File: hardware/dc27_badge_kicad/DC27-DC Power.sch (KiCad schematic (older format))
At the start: 21 parts, among them SW401 POWER ON, U401 MCP73831-2-OT, U402 LM1117-3.3, U403 MAX17043

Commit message: clean up fp libraries
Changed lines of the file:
@@
 U 1 1 5BAA0329
 P 3850 5950
-F 0 "U403" H 3950 6500 50  0000 C CNN
+F 0 "U403" H 4000 6500 50  0000 C CNN
 F 1 "MAX17043" H 4100 6400 50  0000 C CNN
 F 2 "Package_DFN_QFN:DFN-8-1EP_2x3mm_P0.5mm_EP0.61x2.2mm" H 3850 5900 50  0001 C CNN
@@
 $EndComp
 Wire Wire Line
-	4150 4050 4150 4200
-Wire Wire Line
 	4150 3250 3650 3250
 Wire Wire Line
 	3650 3250 3650 3350
-Wire Wire Line
-	3650 4050 3650 4200
 Text Notes 3850 1400 0    50   ~ 0
 500MA LIPO CHARGER\nMCP73831
@@
 Text GLabel 3650 4200 3    50   Input ~ 0
 VBUS
+Wire Wire Line
+	3650 4200 3650 4050
+Wire Wire Line
+	4150 4050 4150 4200
 $EndSCHEMATC

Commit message: add gerbers for prototype
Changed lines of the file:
@@
 Comment4 ""
 $EndDescr
-Text Notes 300  -350 0    79   ~ 16
+Text Notes 1650 1000 0    79   ~ 16
 LiPo Charging and USB Power\n
 $Comp

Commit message: check in all datasheets, BOM tools, and start to get first fab together
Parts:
- removed U403: MAX17043, Package_DFN_QFN:DFN-8-1EP_2x3mm_P0.5mm_EP0.61x2.2mm, symbol max17043:MAX17043
- added C408: 0.47uF, Capacitor_SMD:C_0603_1608Metric, symbol Device:C
- added U403: MAX17055-10-TDFN-EP, SON50P300X300X80-11N:SON50P300X300X80-11N, symbol jna_parts:MAX17055-10-TDFN-EP
- C406: footprint Capacitor_SMD:C_1206_3216Metric -> Capacitor_SMD:C_0603_1608Metric
- C407: value 1.0uF -> 0.1uF
- R401, R402: value R -> 1K
- R404: value 1k -> 0.01, 1%
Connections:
- net labels added: BATT_CSN, BATT_CSP
- wire segments 73 -> 76
- no-connect marks 2 -> 4
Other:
- note added: "Fuel Gauge Circuit\n"
- note added: "MAX17055 user guide seems to indicate that\ni2c slave address is 0x6c\nhttps://pdfserv.maximintegrated.com/en/an/AN6358.pdf"
- note removed: "MAX17043 i2c address 0x36\nCould send ALT to a interrupt pin for power down alerting\nPackage TDFN 8"
- note removed: "OPTIONAL Fuel Gauge Circuit\n"
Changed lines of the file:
@@
 Text Notes 1650 1000 0    79   ~ 16
 LiPo Charging and USB Power\n
-$Comp
-L max17043:MAX17043 U403
-U 1 1 5BAA0329
-P 3850 5950
-F 0 "U403" H 4000 6500 50  0000 C CNN
-F 1 "MAX17043" H 4100 6400 50  0000 C CNN
-F 2 "Package_DFN_QFN:DFN-8-1EP_2x3mm_P0.5mm_EP0.61x2.2mm" H 3850 5900 50  0001 C CNN
-F 3 "" H 3850 5900 50  0001 C CNN
-	1    3850 5950
-	1    0    0    -1
-$EndComp
-$Comp
-L Device:R R404
-U 1 1 5BAA05A1
-P 4700 6050
-F 0 "R404" V 4907 6050 50  0000 C CNN
-F 1 "1k" V 4816 6050 50  0000 C CNN
-F 2 "Resistor_SMD:R_0603_1608Metric" V 4630 6050 50  0001 C CNN
-F 3 "~" H 4700 6050 50  0001 C CNN
-	1    4700 6050
-	0    -1   -1   0
-$EndComp
-Text GLabel 5100 6050 2    50   Input ~ 0
+Text GLabel 5950 5400 2    50   Input ~ 0
 VBATT
-Wire Wire Line
-	4850 6050 5100 6050
-Wire Wire Line
-	4250 6050 4550 6050
-$Comp
-L Device:C C407
-U 1 1 5BAA6C60
-P 2800 5300
-F 0 "C407" H 2915 5346 50  0000 L CNN
-F 1 "1.0uF" H 2915 5255 50  0000 L CNN
-F 2 "Capacitor_SMD:C_0603_1608Metric" H 2838 5150 50  0001 C CNN
-F 3 "~" H 2800 5300 50  0001 C CNN
-	1    2800 5300
-	1    0    0    -1
-$EndComp
-$Comp
-L power:+3.3V #PWR0410
-U 1 1 5BAA710D
-P 2800 5000
-F 0 "#PWR0410" H 2800 4850 50  0001 C CNN
-F 1 "+3.3V" H 2815 5173 50  0000 C CNN
-F 2 "" H 2800 5000 50  0001 C CNN
-F 3 "" H 2800 5000 50  0001 C CNN
-	1    2800 5000
-	1    0    0    -1
-$EndComp
 $Comp
 L power:GND #PWR0413
 U 1 1 5BAADAD5
-P 3500 6650
-F 0 "#PWR0413" H 3500 6400 50  0001 C CNN
-F 1 "GND" H 3505 6477 50  0000 C CNN
-F 2 "" H 3500 6650 50  0001 C CNN
-F 3 "" H 3500 6650 50  0001 C CNN
-	1    3500 6650
-	1    0    0    -1
-$EndComp
-Wire Wire Line
-	3500 6550 3500 6650
-Wire Wire Line
-	3500 6550 3850 6550
-Wire Wire Line
-	3850 6550 3850 6450
-Connection ~ 3500 6550
+P 5650 6150
+F 0 "#PWR0413" H 5650 5900 50  0001 C CNN
+F 1 "GND" H 5655 5977 50  0000 C CNN
+F 2 "" H 5650 6150 50  0001 C CNN
+F 3 "" H 5650 6150 50  0001 C CNN
+	1    5650 6150
+	1    0    0    -1
+$EndComp
 Text Notes 1700 4700 0    50   ~ 10
-OPTIONAL Fuel Gauge Circuit\n
-Wire Wire Line
-	2800 5000 2800 5100
-$Comp
-L power:GND #PWR0411
-U 1 1 5BAB8F83
-P 2800 5550
-F 0 "#PWR0411" H 2800 5300 50  0001 C CNN
-F 1 "GND" H 2650 5400 50  0000 C CNN
-F 2 "" H 2800 5550 50  0001 C CNN
-F 3 "" H 2800 5550 50  0001 C CNN
-	1    2800 5550
-	1    0    0    -1
-$EndComp
-Wire Wire Line
-	2800 5450 2800 5550
-Wire Wire Line
-	3850 5100 2800 5100
-Wire Wire Line
-	3850 5100 3850 5500
-Connection ~ 2800 5100
-Wire Wire Line
-	2800 5100 2800 5150
-Text GLabel 3200 5750 0    50   BiDi ~ 0
+Fuel Gauge Circuit\n
+Text GLabel 3100 5850 0    50   BiDi ~ 0
 I2C_SDA
-Wire Wire Line
-	3200 5750 3450 5750
-Text GLabel 3200 5850 0    50   Input ~ 0
+Text GLabel 3100 5700 0    50   Input ~ 0
 I2C_SCK
-Wire Wire Line
-	3200 5850 3450 5850
-Wire Wire Line
-	3450 5950 2900 5950
-Wire Wire Line
-	2900 6550 3500 6550
-NoConn ~ 3450 6050
-Text Notes 4000 6650 0    50   ~ 0
-MAX17043 i2c address 0x36\nCould send ALT to a interrupt pin for power down alerting\nPackage TDFN 8
-$Comp
-L power:GND #PWR0412
-U 1 1 5BADA991
-P 4400 6150
-F 0 "#PWR0412" H 4400 5900 50  0001 C CNN
-F 1 "GND" H 4405 5977 50  0000 C CNN
-F 2 "" H 4400 6150 50  0001 C CNN
-F 3 "" H 4400 6150 50  0001 C CNN
-	1    4400 6150
-	1    0    0    -1
-$EndComp
-Wire Wire Line
-	4250 5950 4400 5950
-Wire Wire Line
-	4400 5950 4400 6150
-Wire Wire Line
-	2900 5950 2900 6550
+Text Notes 1700 5000 0    50   ~ 0
+MAX17055 user guide seems to indicate that\ni2c slave address is 0x6c\nhttps://pdfserv.maximintegrated.com/en/an/AN6358.pdf
 Text Notes 7350 7500 0    50   ~ 0
 DC 27 Badge - Team Ides - John Adams / Bill Paul
@@
 L power:GND #PWR0408
 U 1 1 5C4653C6
-P 5600 2950
-F 0 "#PWR0408" H 5600 2700 50  0001 C CNN
-F 1 "GND" H 5605 2777 50  0000 C CNN
-F 2 "" H 5600 2950 50  0001 C CNN
-F 3 "" H 5600 2950 50  0001 C CNN
-	1    5600 2950
-	1    0    0    -1
-$EndComp
-Wire Wire Line
-	5600 2650 5600 2950
+P 5600 3500
+F 0 "#PWR0408" H 5600 3250 50  0001 C CNN
+F 1 "GND" H 5605 3327 50  0000 C CNN
+F 2 "" H 5600 3500 50  0001 C CNN
+F 3 "" H 5600 3500 50  0001 C CNN
+	1    5600 3500
+	1    0    0    -1
+$EndComp
 Wire Wire Line
 	5600 2100 5600 2250
@@
 F 0 "C406" H 5050 2800 50  0000 L CNN
 F 1 "1uF" H 5100 2700 50  0000 L CNN
-F 2 "Capacitor_SMD:C_1206_3216Metric" H 5038 2500 50  0001 C CNN
+F 2 "Capacitor_SMD:C_0603_1608Metric" H 5038 2500 50  0001 C CNN
 F 3 "~" H 5000 2650 50  0001 C CNN
 	1    5000 2650
@@
 P 4150 3500
 F 0 "R402" H 4220 3546 50  0000 L CNN
-F 1 "R" H 4220 3455 50  0000 L CNN
+F 1 "1K" H 4220 3455 50  0000 L CNN
 F 2 "Resistor_SMD:R_0603_1608Metric" V 4080 3500 50  0001 C CNN
 F 3 "~" H 4150 3500 50  0001 C CNN
@@
 P 3650 3500
 F 0 "R401" H 3720 3546 50  0000 L CNN
-F 1 "R" H 3720 3455 50  0000 L CNN
+F 1 "1K" H 3720 3455 50  0000 L CNN
 F 2 "Resistor_SMD:R_0603_1608Metric" V 3580 3500 50  0001 C CNN
 F 3 "~" H 3650 3500 50  0001 C CNN
@@
 Wire Wire Line
 	6550 1750 6550 2200
-Connection ~ 6550 2200
-Wire Wire Line
-	6550 2200 7250 2200
 $Comp
 L power:PWR_FLAG #FLG0401
@@
 Wire Wire Line
 	7250 1950 7250 2200
-Connection ~ 7250 2200
 Wire Wire Line
 	7250 2200 7650 2200
@@
 Wire Wire Line
 	4150 4050 4150 4200
+$Comp
+L jna_parts:MAX17055-10-TDFN-EP U403
+U 1 1 5C6B1E26
+P 3950 5600
+F 0 "U403" H 3950 6065 50  0000 C CNN
+F 1 "MAX17055-10-TDFN-EP" H 3950 5974 50  0000 C CNN
+F 2 "SON50P300X300X80-11N:SON50P300X300X80-11N" H 3950 5600 50  0001 C CNN
+F 3 "" H 3950 5600 50  0001 C CNN
+	1    3950 5600
+	1    0    0    -1
+$EndComp
+Wire Wire Line
+	3100 5700 3450 5700
+Wire Wire Line
+	3100 5850 3450 5850
+NoConn ~ 4450 5700
+$Comp
+L Device:C C407
+U 1 1 5C6B96F2
+P 5650 5850
+F 0 "C407" H 5765 5896 50  0000 L CNN
+F 1 "0.1uF" H 5765 5805 50  0000 L CNN
+F 2 "Capacitor_SMD:C_0603_1608Metric" H 5688 5700 50  0001 C CNN
+F 3 "~" H 5650 5850 50  0001 C CNN
+	1    5650 5850
+	1    0    0    -1
+$EndComp
+Wire Wire Line
+	5650 6000 5650 6150
+Wire Wire Line
+	5650 5700 5650 5400
+Connection ~ 5650 5400
+Wire Wire Line
+	5650 5400 5950 5400
+NoConn ~ 4450 5550
+NoConn ~ 3450 5550
+$Comp
+L Device:C C408
+U 1 1 5C6C2F3A
+P 5350 6500
+F 0 "C408" H 5465 6546 50  0000 L CNN
+F 1 "0.47uF" H 5465 6455 50  0000 L CNN
+F 2 "Capacitor_SMD:C_0603_1608Metric" H 5388 6350 50  0001 C CNN
+F 3 "~" H 5350 6500 50  0001 C CNN
+	1    5350 6500
+	1    0    0    -1
+$EndComp
+$Comp
+L power:GND #PWR0410
+U 1 1 5C6C2F95
+P 5350 6800
+F 0 "#PWR0410" H 5350 6550 50  0001 C CNN
+F 1 "GND" H 5355 6627 50  0000 C CNN
+F 2 "" H 5350 6800 50  0001 C CNN
+F 3 "" H 5350 6800 50  0001 C CNN
+	1    5350 6800
+	1    0    0    -1
+$EndComp
+Wire Wire Line
+	5350 6650 5350 6800
+Wire Wire Line
+	5350 5850 5350 6350
+Connection ~ 7250 2200
+Connection ~ 6550 2200
+Wire Wire Line
+	6550 2200 7250 2200
+Text GLabel 5750 3100 2    50   Output ~ 0
+BATT_CSP
+Text GLabel 4750 6000 2    50   Input ~ 0
+BATT_CSP
+Wire Wire Line
+	5600 3100 5750 3100
+Wire Wire Line
+	5600 2650 5600 3100
+Wire Wire Line
+	5750 3350 5600 3350
+Wire Wire Line
+	5600 3350 5600 3500
+$Comp
+L Device:R R404
+U 1 1 5C6CAB81
+P 3900 6500
+F 0 "R404" V 3693 6500 50  0000 C CNN
+F 1 "0.01, 1% " V 3784 6500 50  0000 C CNN
+F 2 "Resistor_SMD:R_0603_1608Metric" V 3830 6500 50  0001 C CNN
+F 3 "~" H 3900 6500 50  0001 C CNN
+	1    3900 6500
+	0    1    1    0
+$EndComp
+Text GLabel 3000 6000 0    50   Input ~ 0
+BATT_CSN
+Wire Wire Line
+	4450 5400 5650 5400
+Wire Wire Line
+	4450 6000 4600 6000
+Wire Wire Line
+	4450 5850 5350 5850
+Text GLabel 5750 3350 2    50   Input ~ 0
+BATT_CSN
+Wire Wire Line
+	4600 6000 4600 6500
+Wire Wire Line
+	4600 6500 4050 6500
+Connection ~ 4600 6000
+Wire Wire Line
+	4600 6000 4750 6000
+Wire Wire Line
+	3750 6500 3400 6500
+Wire Wire Line
+	3400 6500 3400 6000
+Wire Wire Line
+	3400 6000 3450 6000
+Connection ~ 3400 6000
+Wire Wire Line
+	3000 6000 3400 6000
 $EndSCHEMATC

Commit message: check in all of the gerbers and artwork
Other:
- note added: "THIS CIRCUIT IS COMPLETELY WRONG. SHORTING R404 MAKES BATTERY WORK AGAIN. BAD BAD BAD!"
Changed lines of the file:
@@
 Wire Wire Line
 	3000 6000 3400 6000
+Text Notes 1300 6700 0    50   ~ 0
+THIS CIRCUIT IS COMPLETELY WRONG. SHORTING R404 MAKES BATTERY WORK AGAIN. BAD BAD BAD!
 $EndSCHEMATC

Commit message: temporary commit with speaker footprint and removal of fuel gauge
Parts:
- removed C407: 0.1uF, Capacitor_SMD:C_0603_1608Metric, symbol Device:C
- removed C408: 0.47uF, Capacitor_SMD:C_0603_1608Metric, symbol Device:C
- removed R404: 0.01, 1%, Resistor_SMD:R_0603_1608Metric, symbol Device:R
- removed U403: MAX17055-10-TDFN-EP, SON50P300X300X80-11N:SON50P300X300X80-11N, symbol jna_parts:MAX17055-10-TDFN-EP
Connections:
- net labels removed: BATT_CSN, BATT_CSP, I2C_SCK, I2C_SDA
- wire segments 76 -> 56
- no-connect marks 4 -> 1
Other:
- note removed: "Fuel Gauge Circuit\n"
- note removed: "MAX17055 user guide seems to indicate that\ni2c slave address is 0x6c\nhttps://pdfserv.maximintegrated.com/en/an/AN6358.pdf"
- note removed: "THIS CIRCUIT IS COMPLETELY WRONG. SHORTING R404 MAKES BATTERY WORK AGAIN. BAD BAD BAD!"
- moved on the sheet: BT401, C401, C402, C403, C404, C405, C406, D401, D402, R401, R402, R403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

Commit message: add AST-01078 3d model and kicad footprint, check in current budget, update charging circut to MCP73833 instead of MCP73831:
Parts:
- removed U401: MCP73831-2-OT, Package_TO_SOT_SMD:SOT-23-5, symbol Battery_Management:MCP73831-2-OT
- added D403: PWR GOOD, Diode_SMD:D_0603_1608Metric, symbol Device:LED
- added R404: 2.0k, Resistor_SMD:R_0603_1608Metric, symbol Device:R
- added R405: 1K, Resistor_SMD:R_0603_1608Metric, symbol Device:R
- added R406: 10K, Resistor_SMD:R_0603_1608Metric, symbol Device:R
- added U401: MCP73833, Package_SO:MSOP-10_3x3mm_P0.5mm, symbol DC27-badge:MCP73833
- C406: value 1uF -> 10uF
- D401: value CHG -> CHARGED
- D402: value DONE -> CHARGING (ORANGE)
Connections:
- net labels removed: VBATT
- wire segments 56 -> 71
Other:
- note added: "10K = 100mA\n5.0K = 200mA\n2.0K = 500mA\n1.0K = 1000mA\n\nREMOVE R404 or R403 TO SET CHARGER TO 500mA. \nWITH BOTH RESISTORS CHARGING IS 1000mA"
- note added: "1A Lipo Charger"
- note added: "3.3v 800mA LDO\nPackage SOT-223\nMax current 1500mA, typ 1200mA"
- note removed: "3.3v 650mA LDO\nPackage SOT-223"
- note removed: "500MA LIPO CHARGER\nMCP73831"
- moved on the sheet: BT401, C401, C402, C403, C404, C405, C406, D401, D402, R401, R402, R403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

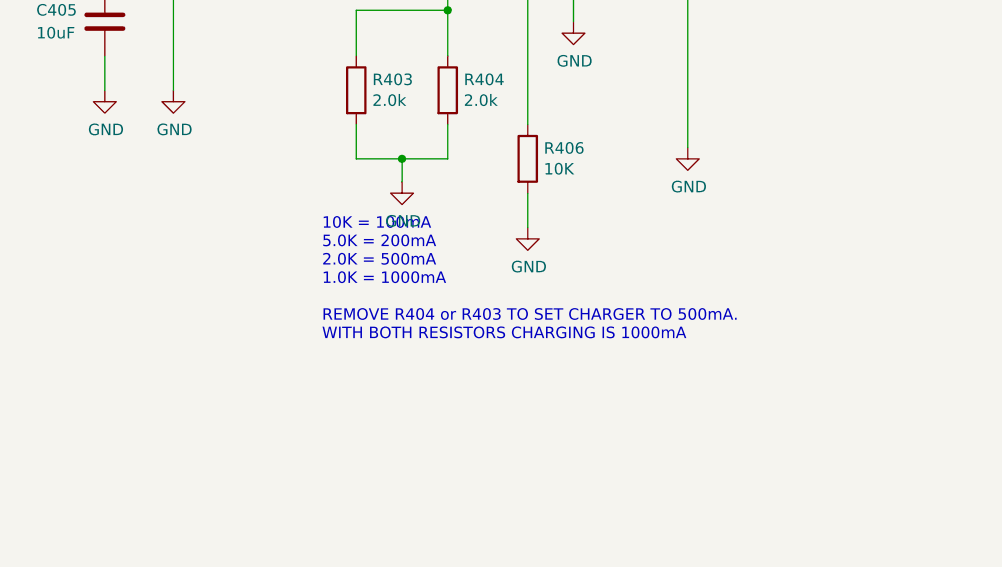
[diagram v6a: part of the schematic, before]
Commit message: add in the new buttons and joystick interrupts, make new schematic for joypads, update the pcb (not done)
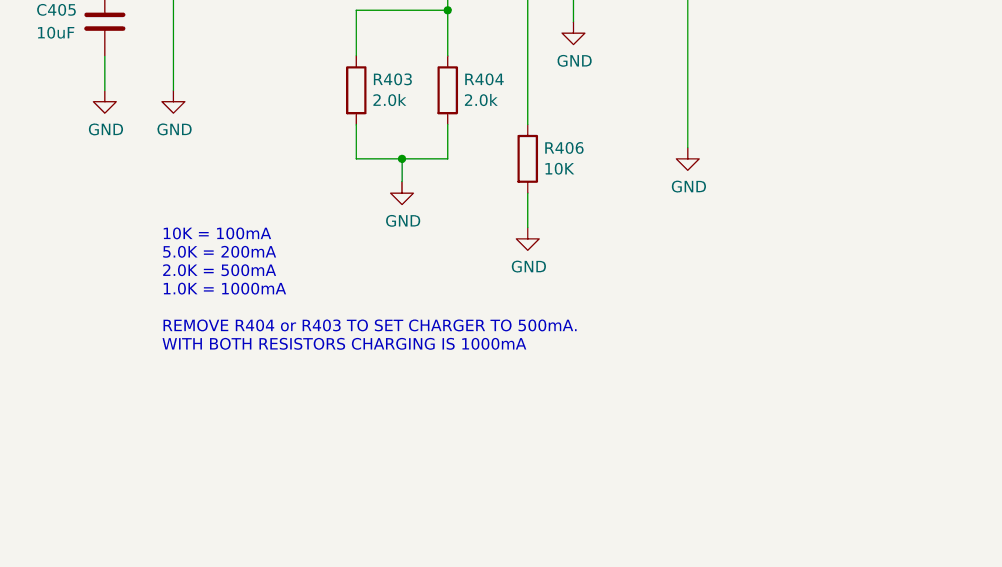
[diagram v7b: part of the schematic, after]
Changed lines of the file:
@@
 $Descr A4 11693 8268
 encoding utf-8
-Sheet 4 7
+Sheet 4 8
 Title ""
 Date ""
@@
 Wire Wire Line
 	2350 2800 2350 3500
-Text Notes 3900 5400 0    50   ~ 0
+Text Notes 3200 5450 0    50   ~ 0
 10K = 100mA\n5.0K = 200mA\n2.0K = 500mA\n1.0K = 1000mA\n\nREMOVE R404 or R403 TO SET CHARGER TO 500mA. \nWITH BOTH RESISTORS CHARGING IS 1000mA
 $Comp

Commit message: Check in V2 of the board. 0 unconnected nets, joypads on pcb
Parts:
- TP401, TP402, TP403: footprint TestPoint:TestPoint_Pad_D2.0mm -> Connector_PinHeader_2.54mm:PinHeader_1x01_P2.54mm_Vertical
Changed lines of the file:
@@
 F 0 "TP402" H 9808 2770 50  0000 L CNN
 F 1 "3.3V TEST" H 9808 2679 50  0000 L CNN
-F 2 "TestPoint:TestPoint_Pad_D2.0mm" H 9950 2650 50  0001 C CNN
+F 2 "Connector_PinHeader_2.54mm:PinHeader_1x01_P2.54mm_Vertical" H 9950 2650 50  0001 C CNN
 F 3 "~" H 9950 2650 50  0001 C CNN
 	1    9750 2650
@@
 F 0 "TP401" H 5358 2720 50  0000 L CNN
 F 1 "VBATT" H 5358 2629 50  0000 L CNN
-F 2 "TestPoint:TestPoint_Pad_D2.0mm" H 5500 2600 50  0001 C CNN
+F 2 "Connector_PinHeader_2.54mm:PinHeader_1x01_P2.54mm_Vertical" H 5500 2600 50  0001 C CNN
 F 3 "~" H 5500 2600 50  0001 C CNN
 	1    5300 2600
@@
 F 0 "TP403" H 10458 2770 50  0000 L CNN
 F 1 "GND" H 10458 2679 50  0000 L CNN
-F 2 "TestPoint:TestPoint_Pad_D2.0mm" H 10600 2650 50  0001 C CNN
+F 2 "Connector_PinHeader_2.54mm:PinHeader_1x01_P2.54mm_Vertical" H 10600 2650 50  0001 C CNN
 F 3 "~" H 10600 2650 50  0001 C CNN
 	1    10400 2650
@@
 Wire Wire Line
 	1500 3150 2950 3150
-Wire Wire Line
-	5500 3700 5500 4550
 $Comp
 L DC27-badge:MCP73833 U401
@@
 Wire Wire Line
 	2950 3150 3450 3150
+Wire Wire Line
+	5500 3700 5500 4550
 $EndSCHEMATC
